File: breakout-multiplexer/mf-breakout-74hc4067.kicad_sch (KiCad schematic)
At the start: 42 parts, among them J1 Conn_01x06_Male, J10 Conn_01x02_Male, J11 Conn_01x02_Male, J12 Conn_01x02_Male, J13 Conn_01x02_Male, J14 Conn_01x02_Male, J15 Conn_01x02_Male, J16 Conn_01x02_Male, J17 Conn_01x02_Male, J18 Conn_01x02_Male, J19 Conn_01x02_Male, J2 Conn_01x06_Male, J20 Conn_01x02_Male, J21 Conn_01x02_Male, J22 Conn_01x02_Male, J23 Conn_01x02_Male, J24 Conn_01x02_Male, J25 Conn_01x02_Male, J26 Conn_01x02_Male, J27 Conn_01x02_Male, J28 Conn_01x02_Male, J29 Conn_01x02_Male, J3 Conn_01x02_Male, J30 Conn_01x02_Male, J31 Conn_01x02_Male, J32 Conn_01x02_Male, J33 Conn_01x02_Male, J34 Conn_01x02_Male, J35 Conn_01x02_Male, J36 Conn_01x02_Male, J4 Conn_01x02_Male, J5 Conn_01x02_Male, J6 Conn_01x02_Male, J7 Conn_01x02_Male, J8 Conn_01x02_Male, J9 Conn_01x02_Male

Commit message: Updated the multiplexer breakout board to v1.2 with better labels, and a QR code
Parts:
- H1, H2, H3, H4: footprint MountingHole:MountingHole_3.2mm_M3 -> MountingHole:MountingHole_3.5mm; now left out of the parts list
- J1, J2: JLC Rotation Offset (none) -> 0; LCSC (none) -> C144397
- J10, J11, J12, J13, J14, J15, J16, J17, J18, J19, J20, J21, J22, J23, J24, J25, J26, J27, J28, J29, J3, J30, J31, J32, J33, J34, J35, J36, J4, J5, J6, J7, J8, J9: JLC Rotation Offset (none) -> 180; LCSC (none) -> C158012
- MUX1, MUX2: footprint common:74HC4067 -> footprints:74HC4067; now left out of the parts list

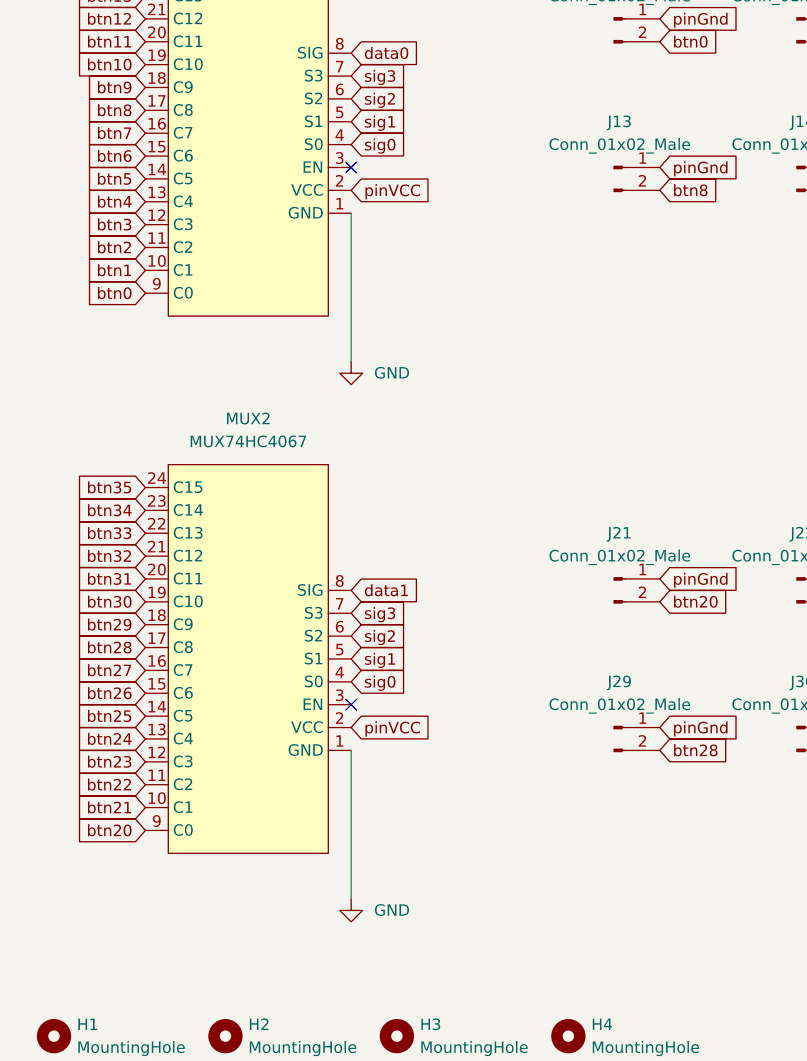
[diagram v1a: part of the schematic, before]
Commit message: multiplexer board v1.4 changes
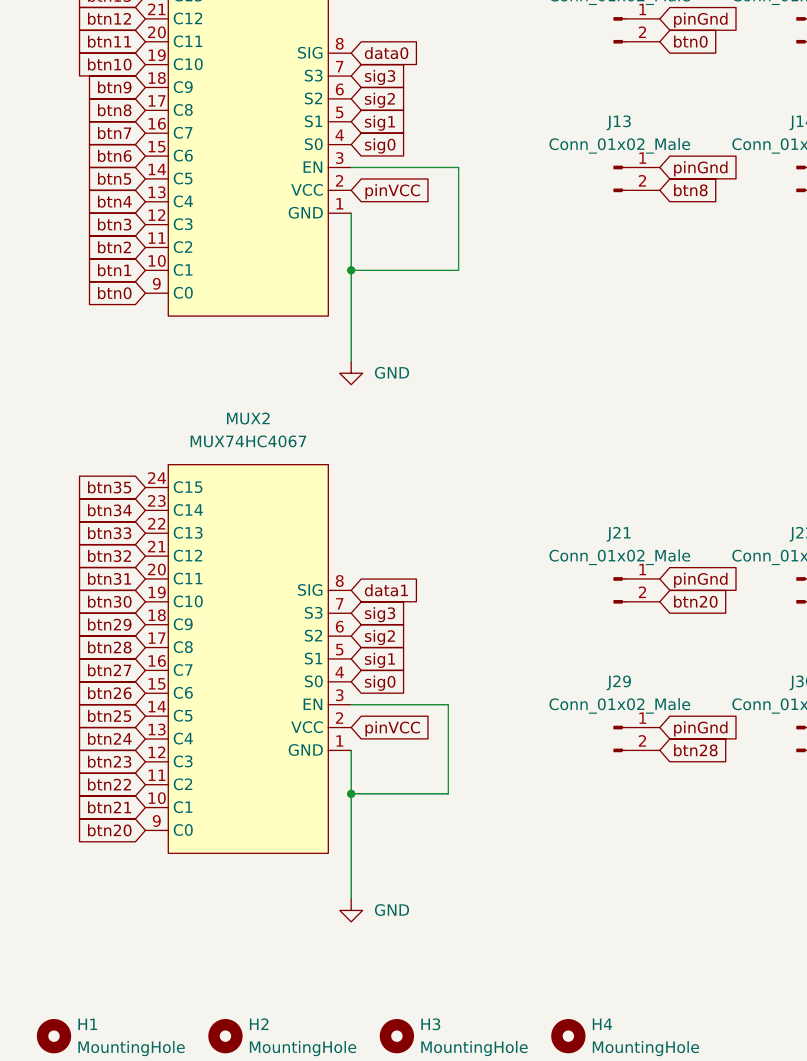
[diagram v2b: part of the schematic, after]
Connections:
- net GND: now also MUX1.3 (EN), MUX2.3 (EN)
- no-connect marks 2 -> 0
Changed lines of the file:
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@@
   (junction (at 85.09 24.13) (diameter 0) (color 0 0 0 0)
   )
-  (no_connect (at 64.77 86.36))
-  (no_connect (at 64.77 146.05))
+  (junction (at 64.77 97.79) (diameter 0) (color 0 0 0 0)
+  )
+  (junction (at 64.77 155.956) (diameter 0) (color 0 0 0 0)
+  )
   (wire (pts (xy 71.12 24.13) (xy 85.09 24.13))
+    (stroke (width 0) (type default) (color 0 0 0 0))
+  )
+  (wire (pts (xy 76.708 97.79) (xy 64.77 97.79))
+    (stroke (width 0) (type default) (color 0 0 0 0))
+  )
+  (wire (pts (xy 64.77 155.956) (xy 64.77 167.64))
+    (stroke (width 0) (type default) (color 0 0 0 0))
+  )
+  (wire (pts (xy 64.77 91.44) (xy 64.77 97.79))
     (stroke (width 0) (type default) (color 0 0 0 0))
   )
@@
     (stroke (width 0) (type default) (color 0 0 0 0))
   )
+  (wire (pts (xy 64.77 97.79) (xy 64.77 107.95))
+    (stroke (width 0) (type default) (color 0 0 0 0))
+  )
   (wire (pts (xy 257.048 33.782) (xy 257.048 37.846))
     (stroke (width 0) (type default) (color 0 0 0 0))
   )
-  (wire (pts (xy 64.77 91.44) (xy 64.77 107.95))
+  (wire (pts (xy 75.565 146.05) (xy 75.565 155.956))
+    (stroke (width 0) (type default) (color 0 0 0 0))
+  )
+  (wire (pts (xy 64.77 155.956) (xy 75.565 155.956))
+    (stroke (width 0) (type default) (color 0 0 0 0))
+  )
+  (wire (pts (xy 64.77 86.36) (xy 76.708 86.36))
+    (stroke (width 0) (type default) (color 0 0 0 0))
+  )
+  (wire (pts (xy 76.708 86.36) (xy 76.708 97.79))
+    (stroke (width 0) (type default) (color 0 0 0 0))
+  )
+  (wire (pts (xy 64.77 146.05) (xy 75.565 146.05))
     (stroke (width 0) (type default) (color 0 0 0 0))
   )
@@
     (stroke (width 0) (type default) (color 0 0 0 0))
   )
-  (wire (pts (xy 64.77 151.13) (xy 64.77 167.64))
+  (wire (pts (xy 64.77 151.13) (xy 64.77 155.956))
     (stroke (width 0) (type default) (color 0 0 0 0))
   )

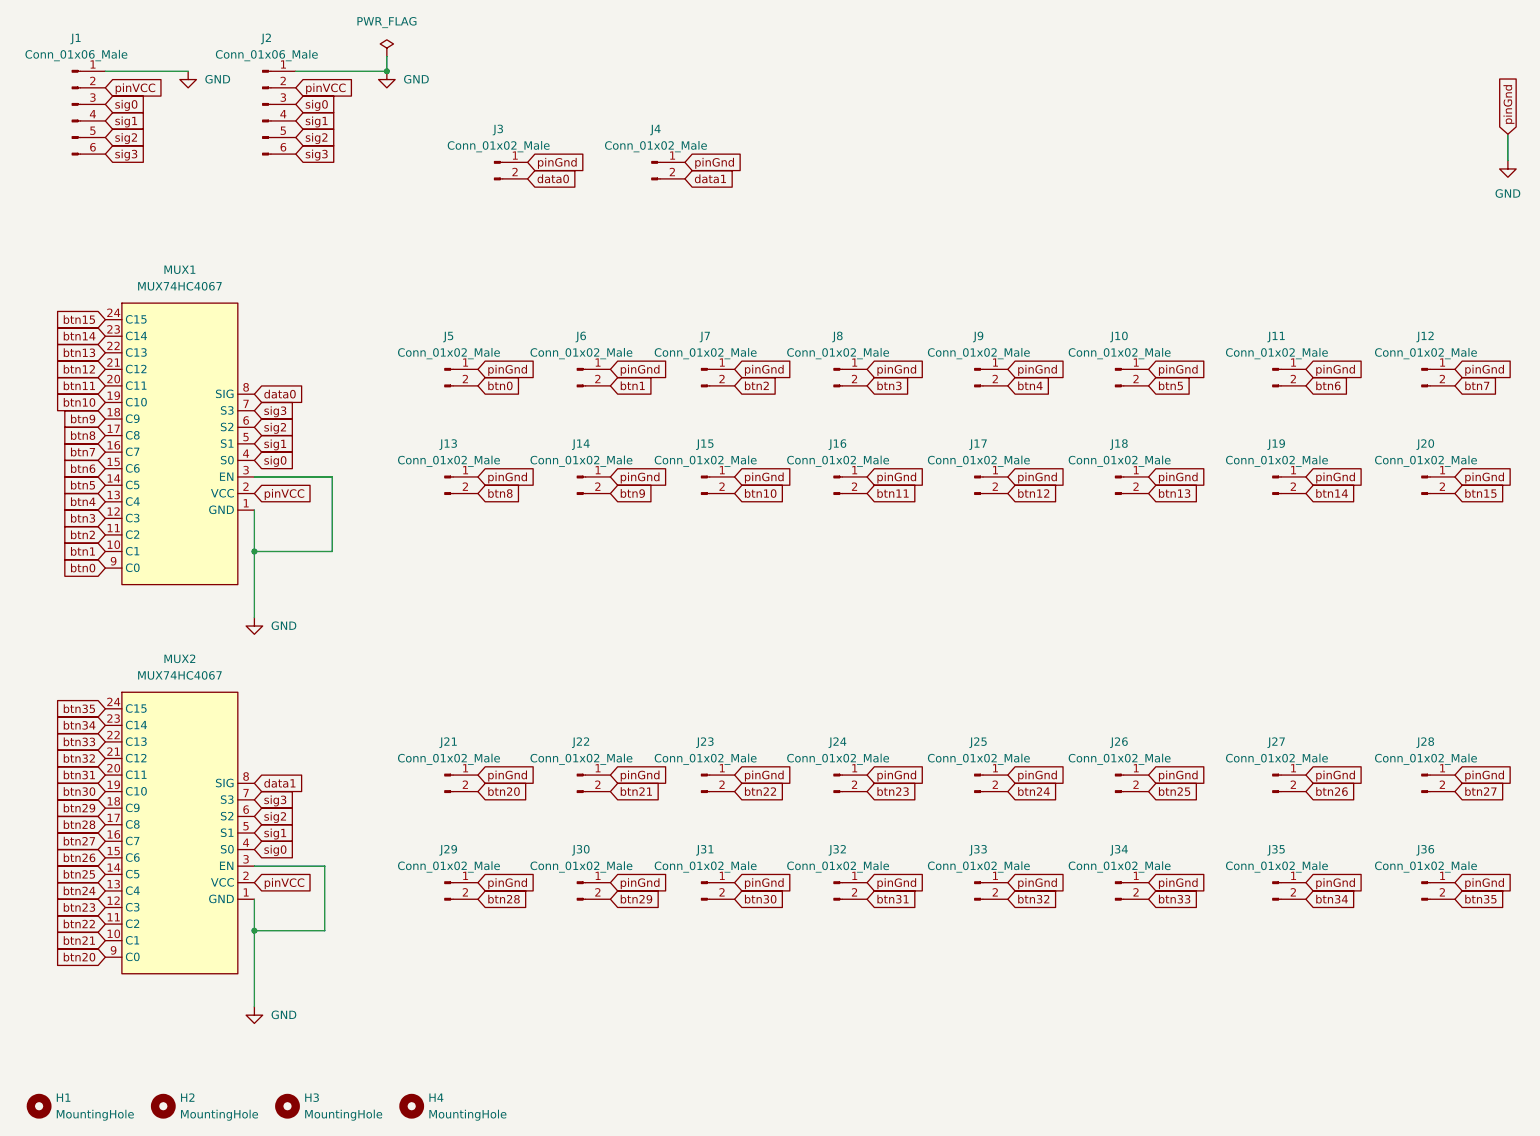
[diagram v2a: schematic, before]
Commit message: 35 standardize mux (#36)
* fixed mounting holes and track width

* Add footprints to library

* Updated 74HC4067 footprints, track size

* not sure :D
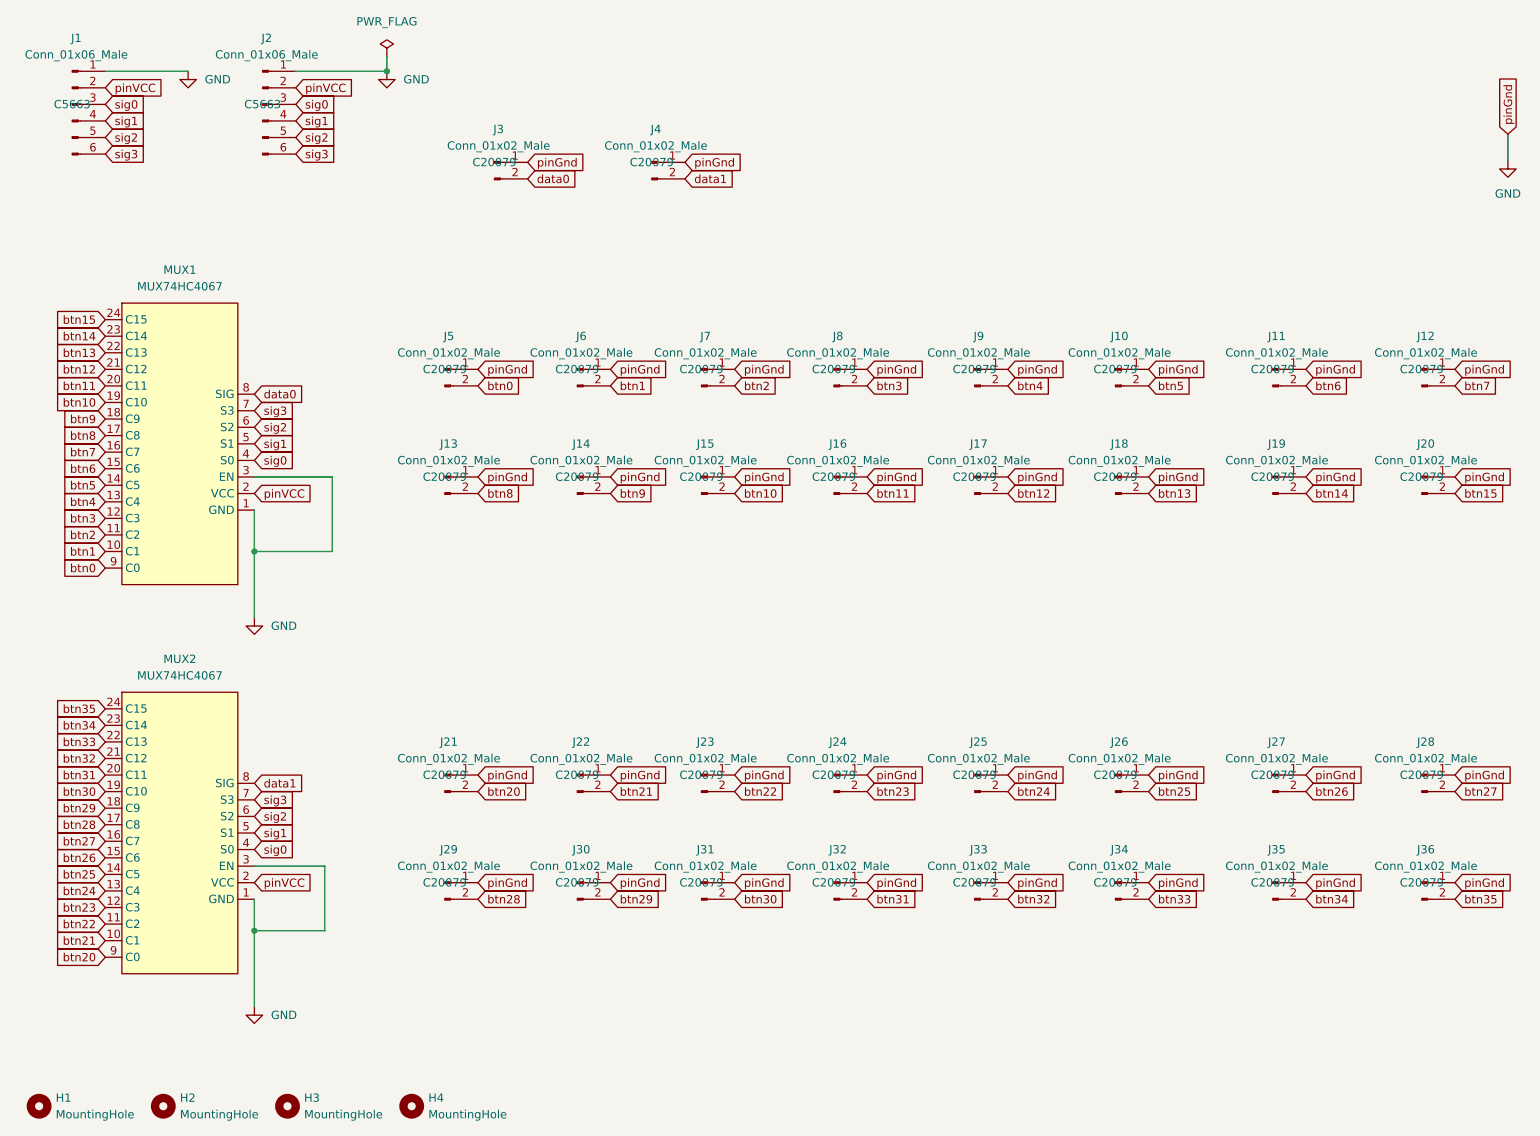
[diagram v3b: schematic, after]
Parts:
- H1, H2, H3, H4: footprint MountingHole:MountingHole_3.5mm -> MountingHole:MountingHole_3.5mm_Pad
- J1, J2: LCSC C144397 -> (none); MPN (none) -> C5663
- J10, J11, J12, J13, J14, J15, J16, J17, J18, J19, J20, J21, J22, J23, J24, J25, J26, J27, J28, J29, J3, J30, J31, J32, J33, J34, J35, J36, J4, J5, J6, J7, J8, J9: LCSC C158012 -> (none); MPN (none) -> C20079
- MUX1, MUX2: footprint footprints:74HC4067 -> MobiFlight:74HC4067
